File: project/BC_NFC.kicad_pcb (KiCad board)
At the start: 2 copper layers, 86 x 54 mm, 12 parts, among them U1 NT3H1101W0FHKH

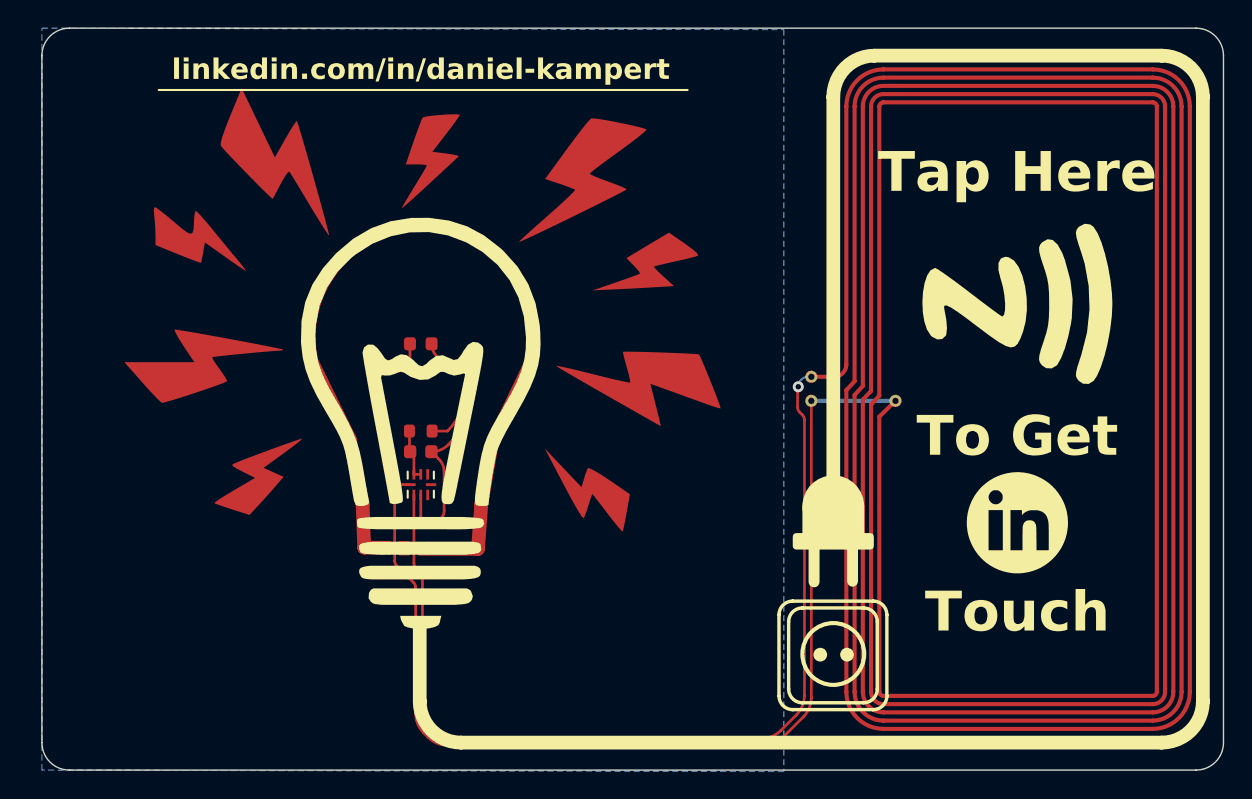
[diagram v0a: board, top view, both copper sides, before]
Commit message: Increase width to 87 mm and add a bit more material between the strap hole and the outer edge
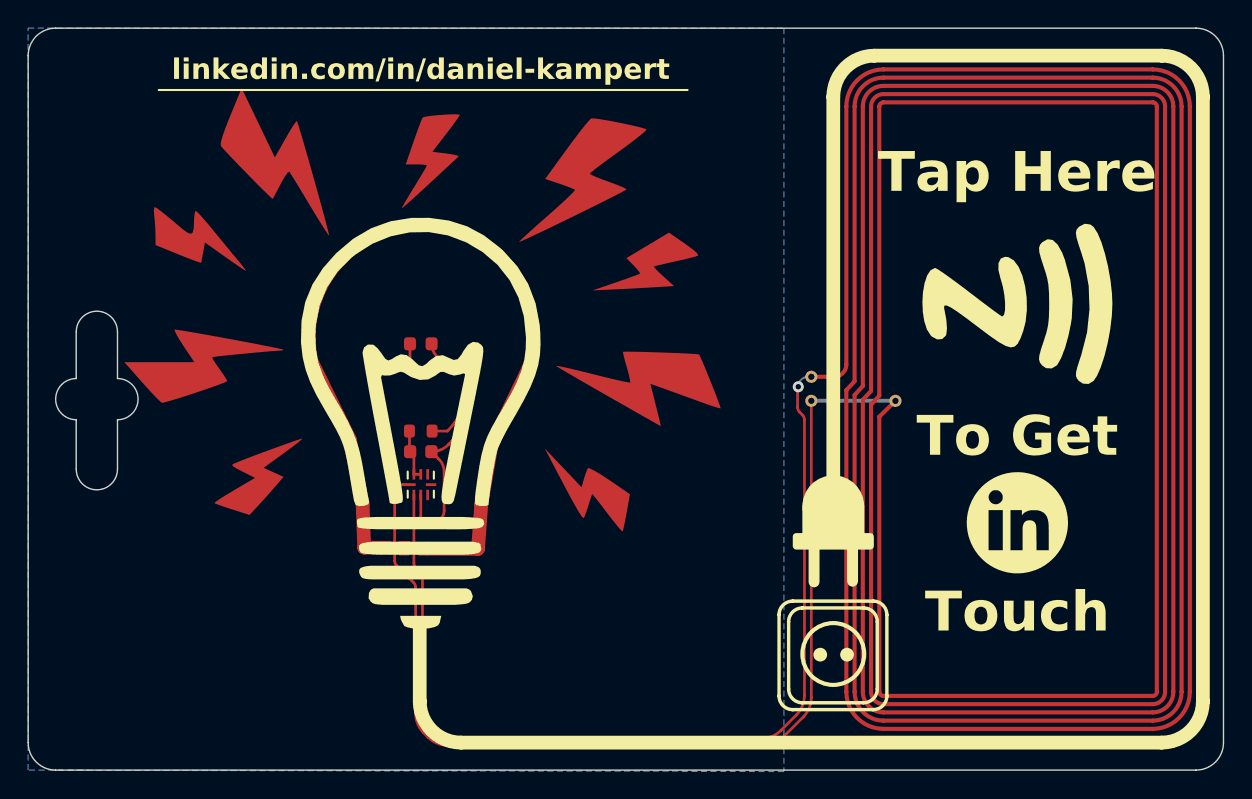
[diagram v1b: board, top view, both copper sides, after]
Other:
- board size 86 x 54 mm -> 87 x 54 mm
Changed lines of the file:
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@@
 	(generator_version "8.99")
 	(general
-		(thickness 1.6)
+		(thickness 1.09)
 		(legacy_teardrops no)
 	)
@@
 				(type "core")
 				(color "FR4 natural")
-				(thickness 1.51)
+				(thickness 1)
 				(material "FR4")
 				(epsilon_r 4.5)
@@
 			)
 		)
-		(dimension
-			(type aligned)
-			(layer "User.1")
-			(pts
-				(xy 171.1 104.45) (xy 171.1 61.55)
-			)
-			(height -11.136426)
-			(gr_text "42,9000 mm"
-				(at 159 83 90)
-				(layer "User.1")
-				(effects
-					(font
-						(size 1 1)
-						(thickness 0.15)
-					)
-				)
-			)
-			(format
-				(prefix "")
-				(suffix "")
-				(units 3)
-				(units_format 1)
-				(precision 4)
-			)
-			(style
-				(thickness 0.1)
-				(arrow_length 1.27)
-				(text_position_mode 2)
-				(extension_height 0.58642)
-				(extension_offset 0.5) keep_text_aligned)
-		)
-		(dimension
-			(type aligned)
-			(layer "User.1")
-			(pts
-				(xy 171.1 61.55) (xy 191 61.55)
-			)
-			(height -7.1)
-			(gr_text "19,9000 mm"
-				(at 181.05 53.3 0)
-				(layer "User.1")
-				(effects
-					(font
-						(size 1 1)
-						(thickness 0.15)
-					)
-				)
-			)
-			(format
-				(prefix "")
-				(suffix "")
-				(units 3)
-				(units_format 1)
-				(precision 4)
-			)
-			(style
-				(thickness 0.1)
-				(arrow_length 1.27)
-				(text_position_mode 0)
-				(extension_height 0.58642)
-				(extension_offset 0.5) keep_text_aligned)
-		)
-		(dimension
-			(type aligned)
-			(layer "User.1")
-			(pts
-				(xy 168.4 58.85) (xy 193.7 58.85)
-			)
-			(height -7.433034)
-			(gr_text "25,3000 mm"
-				(at 181.05 50.266966 0)
-				(layer "User.1")
-				(effects
-					(font
-						(size 1 1)
-						(thickness 0.15)
-					)
-				)
-			)
-			(format
-				(prefix "")
-				(suffix "")
-				(units 3)
-				(units_format 1)
-				(precision 4)
-			)
-			(style
-				(thickness 0.1)
-				(arrow_length 1.27)
-				(text_position_mode 0)
-				(extension_height 0.58642)
-				(extension_offset 0.5) keep_text_aligned)
-		)
-		(dimension
-			(type aligned)
-			(layer "User.1")
-			(pts
-				(xy 168.4 107.15) (xy 168.4 58.85)
-			)
-			(height -11.415778)
-			(gr_text "48,3000 mm"
-				(at 156 82.45 90)
-				(layer "User.1")
-				(effects
-					(font
-						(size 1 1)
-						(thickness 0.15)
-					)
-				)
-			)
-			(format
-				(prefix "")
-				(suffix "")
-				(units 3)
-				(units_format 1)
-				(precision 4)
-			)
-			(style
-				(thickness 0.1)
-				(arrow_length 1.27)
-				(text_position_mode 2)
-				(extension_height 0.58642)
-				(extension_offset 0.5) keep_text_aligned)
-		)
 		(pad "1" thru_hole circle
 			(at 2.075 -18 90)
@@
 		(layer "B.SilkS")
 	)
+	(gr_line
+		(start 112.5 88.1)
+		(end 112.5 84.5)
+		(stroke
+			(width 0.1)
+			(type default)
+		)
+		(layer "Edge.Cuts")
+	)
 	(gr_arc
 		(start 196 108)
@@
 	(gr_line
 		(start 194 56)
-		(end 112 56)
+		(end 111 56)
 		(stroke
 			(width 0.1)
@@
 		(layer "Edge.Cuts")
 	)
+	(gr_line
+		(start 115.5 88.1)
+		(end 115.5 84.5)
+		(stroke
+			(width 0.1)
+			(type default)
+		)
+		(layer "Edge.Cuts")
+	)
+	(gr_arc
+		(start 115.5 81.5)
+		(mid 117 83)
+		(end 115.5 84.5)
+		(stroke
+			(width 0.1)
+			(type default)
+		)
+		(layer "Edge.Cuts")
+	)
+	(gr_arc
+		(start 112.5 84.5)
+		(mid 111 83)
+		(end 112.5 81.5)
+		(stroke
+			(width 0.1)
+			(type default)
+		)
+		(layer "Edge.Cuts")
+	)
 	(gr_arc
-		(start 110 58)
-		(mid 110.585786 56.585786)
-		(end 112 56)
+		(start 112.5 78.1)
+		(mid 114 76.6)
+		(end 115.5 78.1)
+		(stroke
+			(width 0.1)
+			(type default)
+		)
+		(layer "Edge.Cuts")
+	)
+	(gr_arc
+		(start 109 58)
+		(mid 109.585786 56.585786)
+		(end 111 56)
+		(stroke
+			(width 0.1)
+			(type default)
+		)
+		(layer "Edge.Cuts")
+	)
+	(gr_arc
+		(start 115.5 88.1)
+		(mid 114 89.6)
+		(end 112.5 88.1)
 		(stroke
 			(width 0.1)
@@
 	)
 	(gr_line
-		(start 110 58)
-		(end 110 108)
+		(start 109 58)
+		(end 109 108)
 		(stroke
 			(width 0.1)
@@
 	)
 	(gr_line
-		(start 112 110)
+		(start 115.5 81.5)
+		(end 115.5 78.1)
+		(stroke
+			(width 0.1)
+			(type default)
+		)
+		(layer "Edge.Cuts")
+	)
+	(gr_line
+		(start 111 110)
 		(end 194 110)
 		(stroke
@@
 	)
 	(gr_arc
-		(start 112 110)
-		(mid 110.585786 109.414214)
-		(end 110 108)
+		(start 111 110)
+		(mid 109.585786 109.414214)
+		(end 109 108)
+		(stroke
+			(width 0.1)
+			(type default)
+		)
+		(layer "Edge.Cuts")
+	)
+	(gr_line
+		(start 112.5 78.1)
+		(end 112.5 81.5)
 		(stroke
 			(width 0.1)
@@
 		(layer "User.1")
 		(pts
-			(xy 196 83) (xy 110 83)
+			(xy 153 56) (xy 153 110)
 		)
-		(height 37.499999)
-		(gr_text "86,0000 mm"
-			(at 153 44.350001 0)
+		(height 52)
+		(gr_text "54,0000 mm"
+			(at 99.85 83 90)
 			(layer "User.1")
 			(effects
@@
 	)
 	(dimension
-		(type aligned)
-		(layer "User.1")
+		(type orthogonal)
+		(layer "Dwgs.User")
 		(pts
-			(xy 153 56) (xy 153 110)
+			(xy 109 108) (xy 196 108)
 		)
-		(height 52)
-		(gr_text "54,0000 mm"
-			(at 99.85 83 90)
-			(layer "User.1")
+		(height 8)
+		(orientation 0)
+		(gr_text "87,0000 mm"
+			(at 152.5 114.85 0)
+			(layer "Dwgs.User")
 			(effects
 				(font
@@
 		)
 		(style
-			(thickness 0.15)
+			(thickness 0.1)
 			(arrow_length 1.27)
 			(text_position_mode 0)
@@
 		(polygon
 			(pts
-				(xy 164 56.1) (xy 164 110.1) (xy 110 110) (xy 110 56)
+				(xy 164 56) (xy 164 110.1) (xy 109 110) (xy 109 56)
 			)
 		)
